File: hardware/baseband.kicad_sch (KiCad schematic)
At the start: 36 parts, among them U501 MCP4551-103, U502 MCP455x, U6 MCP6002, U7 MCP6002

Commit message: Replaced pkl footprints with kicad standard library footprints
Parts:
- C45, C48, C49, C501, C502, C51, C52, C53, C55, C60: footprint pkl_dipol:C_0603 -> Capacitor_SMD:C_0603_1608Metric
- R36, R37, R38, R39, R40, R41, R42, R43, R45, R46, R52, R55: footprint pkl_dipol:R_0603 -> Resistor_SMD:R_0603_1608Metric
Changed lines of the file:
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@@
       (effects (font (size 1.27 1.27)) (justify left))
     )
-    (property "Footprint" "pkl_dipol:R_0603" (at 180.34 36.83 0)
+    (property "Footprint" "Resistor_SMD:R_0603_1608Metric" (at 180.34 36.83 0)
       (effects (font (size 1.524 1.524)) hide)
     )
@@
       (effects (font (size 1.27 1.27)) (justify left))
     )
-    (property "Footprint" "pkl_dipol:R_0603" (at 185.42 68.58 0)
+    (property "Footprint" "Resistor_SMD:R_0603_1608Metric" (at 185.42 68.58 0)
       (effects (font (size 1.524 1.524)) hide)
     )
@@
       (effects (font (size 1.27 1.27)) (justify left))
     )
-    (property "Footprint" "pkl_dipol:C_0603" (at 206.375 39.37 0)
+    (property "Footprint" "Capacitor_SMD:C_0603_1608Metric" (at 206.375 39.37 0)
       (effects (font (size 1.524 1.524)) hide)
     )
@@
       (effects (font (size 1.27 1.27)) (justify left))
     )
-    (property "Footprint" "pkl_dipol:C_0603" (at 146.05 133.35 0)
+    (property "Footprint" "Capacitor_SMD:C_0603_1608Metric" (at 146.05 133.35 0)
       (effects (font (size 1.524 1.524)) hide)
     )
@@
       (effects (font (size 1.27 1.27)) (justify left))
     )
-    (property "Footprint" "pkl_dipol:C_0603" (at 93.98 44.45 0)
+    (property "Footprint" "Capacitor_SMD:C_0603_1608Metric" (at 93.98 44.45 0)
       (effects (font (size 1.524 1.524)) hide)
     )
@@
       (effects (font (size 1.27 1.27)) (justify left))
     )
-    (property "Footprint" "pkl_dipol:R_0603" (at 175.26 58.42 0)
+    (property "Footprint" "Resistor_SMD:R_0603_1608Metric" (at 175.26 58.42 0)
       (effects (font (size 1.524 1.524)) hide)
     )
@@
       (effects (font (size 1.27 1.27)))
     )
-    (property "Footprint" "pkl_dipol:R_0603" (at 99.06 39.37 0)
+    (property "Footprint" "Resistor_SMD:R_0603_1608Metric" (at 99.06 39.37 0)
       (effects (font (size 1.524 1.524)) hide)
     )
@@
       (effects (font (size 1.27 1.27)) (justify left))
     )
-    (property "Footprint" "pkl_dipol:R_0603" (at 185.42 58.42 0)
+    (property "Footprint" "Resistor_SMD:R_0603_1608Metric" (at 185.42 58.42 0)
       (effects (font (size 1.524 1.524)) hide)
     )
@@
       (effects (font (size 1.27 1.27)))
     )
-    (property "Footprint" "pkl_dipol:R_0603" (at 119.38 39.37 0)
+    (property "Footprint" "Resistor_SMD:R_0603_1608Metric" (at 119.38 39.37 0)
       (effects (font (size 1.524 1.524)) hide)
     )
@@
       (effects (font (size 1.27 1.27)) (justify right))
     )
-    (property "Footprint" "pkl_dipol:C_0603" (at 53.975 161.29 0)
+    (property "Footprint" "Capacitor_SMD:C_0603_1608Metric" (at 53.975 161.29 0)
       (effects (font (size 1.27 1.27)) hide)
     )
@@
       (effects (font (size 1.27 1.27)) (justify left))
     )
-    (property "Footprint" "pkl_dipol:R_0603" (at 139.7 80.645 0)
+    (property "Footprint" "Resistor_SMD:R_0603_1608Metric" (at 139.7 80.645 0)
       (effects (font (size 1.524 1.524)) hide)
     )
@@
       (effects (font (size 1.27 1.27)) (justify left))
     )
-    (property "Footprint" "pkl_dipol:R_0603" (at 180.34 26.67 0)
+    (property "Footprint" "Resistor_SMD:R_0603_1608Metric" (at 180.34 26.67 0)
       (effects (font (size 1.524 1.524)) hide)
     )
@@
       (effects (font (size 1.27 1.27)) (justify left))
     )
-    (property "Footprint" "pkl_dipol:C_0603" (at 114.3 44.45 0)
+    (property "Footprint" "Capacitor_SMD:C_0603_1608Metric" (at 114.3 44.45 0)
       (effects (font (size 1.524 1.524)) hide)
     )
@@
       (effects (font (size 1.27 1.27)))
     )
-    (property "Footprint" "pkl_dipol:C_0603" (at 140.97 119.38 0)
+    (property "Footprint" "Capacitor_SMD:C_0603_1608Metric" (at 140.97 119.38 0)
       (effects (font (size 1.524 1.524)) hide)
     )
@@
       (effects (font (size 1.27 1.27)))
     )
-    (property "Footprint" "pkl_dipol:R_0603" (at 120.65 128.27 0)
+    (property "Footprint" "Resistor_SMD:R_0603_1608Metric" (at 120.65 128.27 0)
       (effects (font (size 1.524 1.524)) hide)
     )
@@
       (effects (font (size 1.27 1.27)))
     )
-    (property "Footprint" "pkl_dipol:C_0603" (at 86.36 27.94 0)
+    (property "Footprint" "Capacitor_SMD:C_0603_1608Metric" (at 86.36 27.94 0)
       (effects (font (size 1.524 1.524)) hide)
     )
@@
       (effects (font (size 1.27 1.27)))
     )
-    (property "Footprint" "pkl_dipol:R_0603" (at 109.22 39.37 0)
+    (property "Footprint" "Resistor_SMD:R_0603_1608Metric" (at 109.22 39.37 0)
       (effects (font (size 1.524 1.524)) hide)
     )
@@
       (effects (font (size 1.27 1.27)) (justify left))
     )
-    (property "Footprint" "pkl_dipol:C_0603" (at 215.9 129.54 0)
+    (property "Footprint" "Capacitor_SMD:C_0603_1608Metric" (at 215.9 129.54 0)
       (effects (font (size 1.524 1.524)) hide)
     )
@@
       (effects (font (size 1.27 1.27)))
     )
-    (property "Footprint" "pkl_dipol:R_0603" (at 140.97 128.27 0)
+    (property "Footprint" "Resistor_SMD:R_0603_1608Metric" (at 140.97 128.27 0)
       (effects (font (size 1.524 1.524)) hide)
     )
@@
       (effects (font (size 1.27 1.27)) (justify left))
     )
-    (property "Footprint" "pkl_dipol:C_0603" (at 125.73 133.35 0)
+    (property "Footprint" "Capacitor_SMD:C_0603_1608Metric" (at 125.73 133.35 0)
       (effects (font (size 1.524 1.524)) hide)
     )
@@
       (effects (font (size 1.27 1.27)))
     )
-    (property "Footprint" "pkl_dipol:R_0603" (at 130.81 128.27 0)
+    (property "Footprint" "Resistor_SMD:R_0603_1608Metric" (at 130.81 128.27 0)
       (effects (font (size 1.524 1.524)) hide)
     )
@@
       (effects (font (size 1.27 1.27)) (justify right))
     )
-    (property "Footprint" "pkl_dipol:C_0603" (at 74.295 76.835 0)
-      (effects (font (size 1.27 1.27)) hide)
-    )
+    (property "Footprint" "Capacitor_SMD:C_0603_1608Metric" (at 74.295 76.835 0)
+      (effects (font (size 1.27 1.27)) hide)
+    )

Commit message: Updated title blocks
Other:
- company: (none) -> M17Project
- title: (none) -> Module17
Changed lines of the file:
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@@
 (kicad_sch (version 20230121) (generator eeschema)
   (paper "A4")
+  (title_block
+    (title "Module17")
+    (date "2023-12-06")
+    (rev "Rev 0.99")
+    (company "M17Project")
+    (comment 1 "Morgan ON4MOD")
+    (comment 2 "Mathis - DB9MAT")
+    (comment 3 "Wojciech - SP5WWP")
+  )
   (junction (at 115.57 128.27) (diameter 1.016) (color 0 0 0 0)
   )

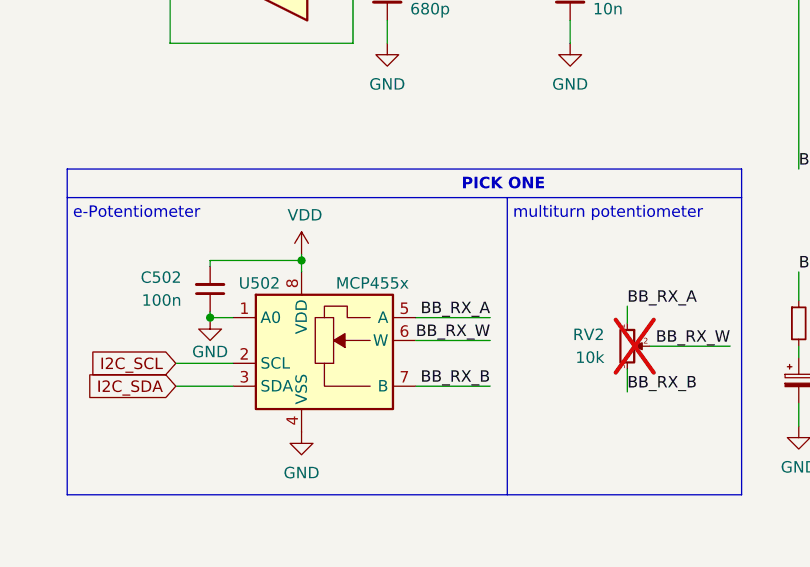
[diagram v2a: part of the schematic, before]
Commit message: Updated some components values
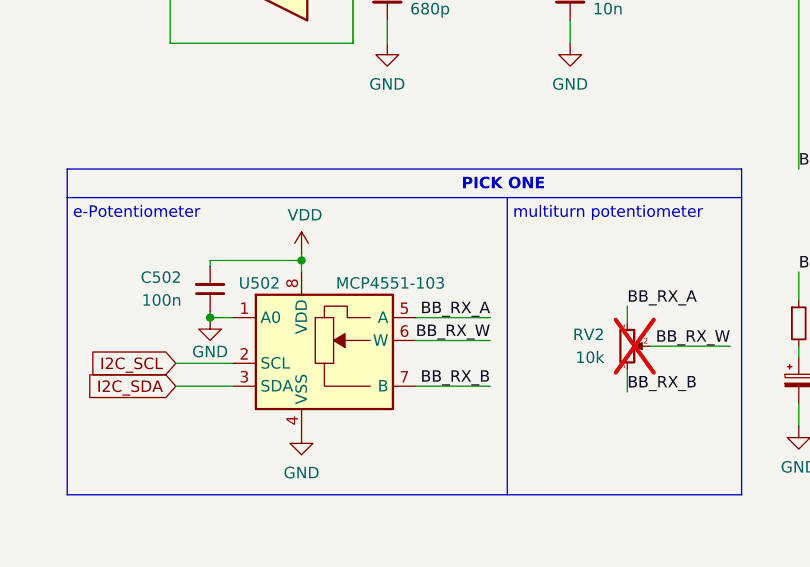
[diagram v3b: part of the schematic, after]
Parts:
- U502: value MCP455x -> MCP4551-103
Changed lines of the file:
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@@
       (effects (font (size 1.27 1.27)) (justify left))
     )
-    (property "Value" "MCP455x" (at 88.265 76.2 0)
+    (property "Value" "MCP4551-103" (at 88.265 76.2 0)
       (effects (font (size 1.27 1.27)) (justify left))
     )
